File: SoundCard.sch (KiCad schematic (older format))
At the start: 44 parts, among them J1 Conn_Coaxial_inv, J2 Conn_01x03_Female, J3 Conn_01x03_Female, P1 CONN_36_P1.00_PCI, U1 LM334M, U2 LM1972, U3 OPA2388IDGK, U4 TLV320ADC6140, U5 TPS7A90

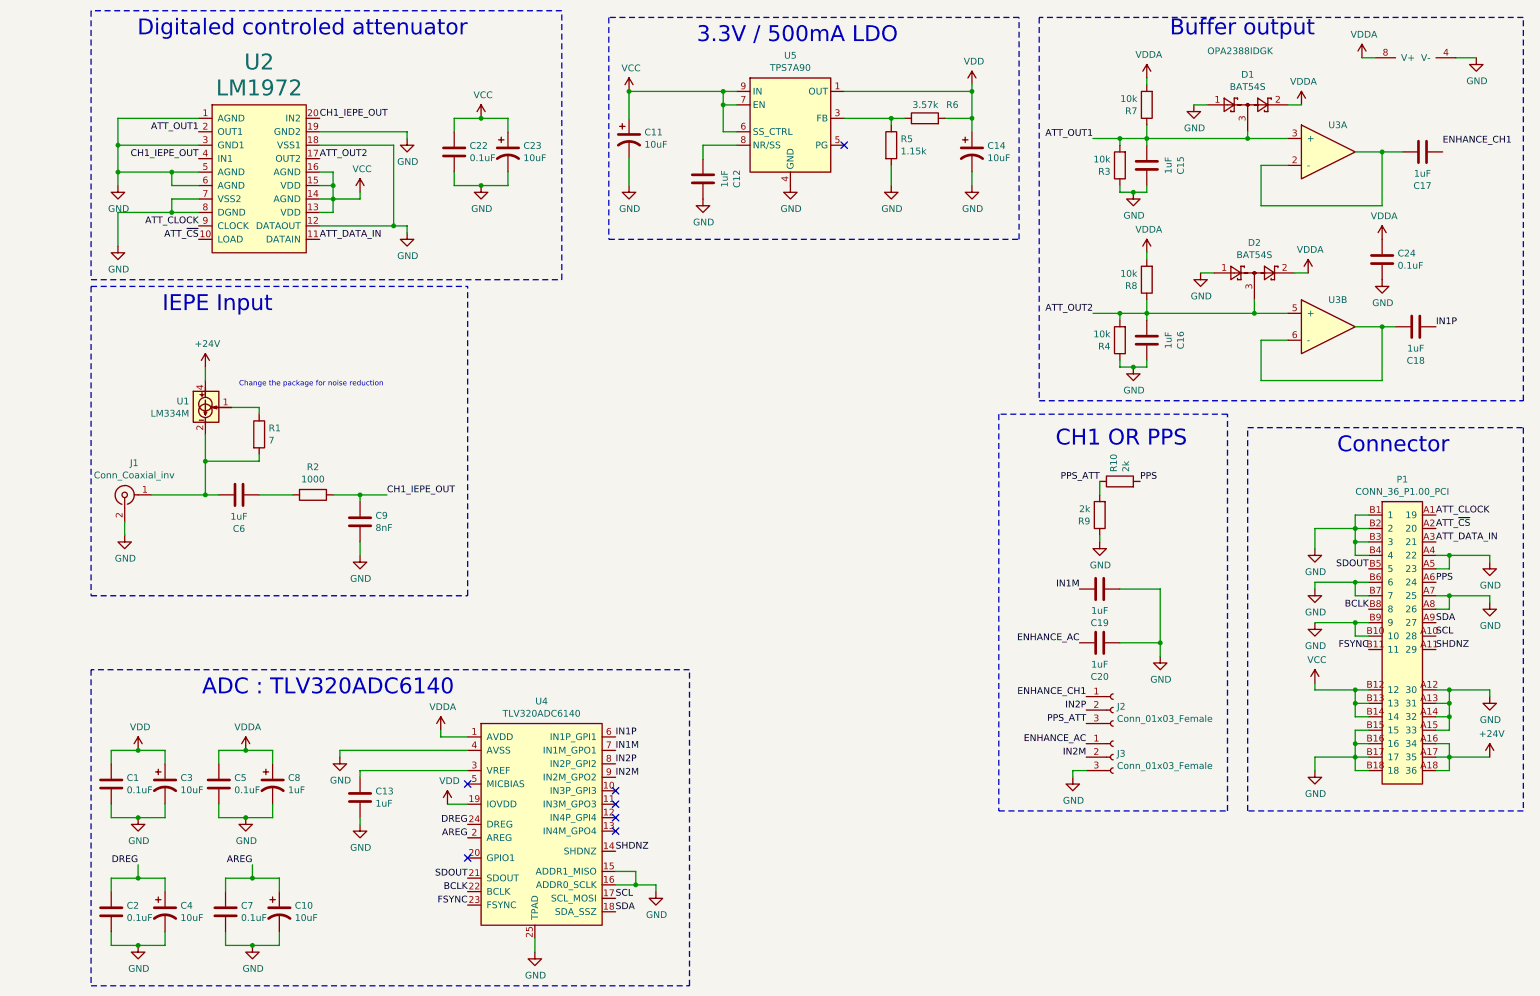
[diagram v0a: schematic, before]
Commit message: Adding 1.65V LDO for Recommon voltage of AOP
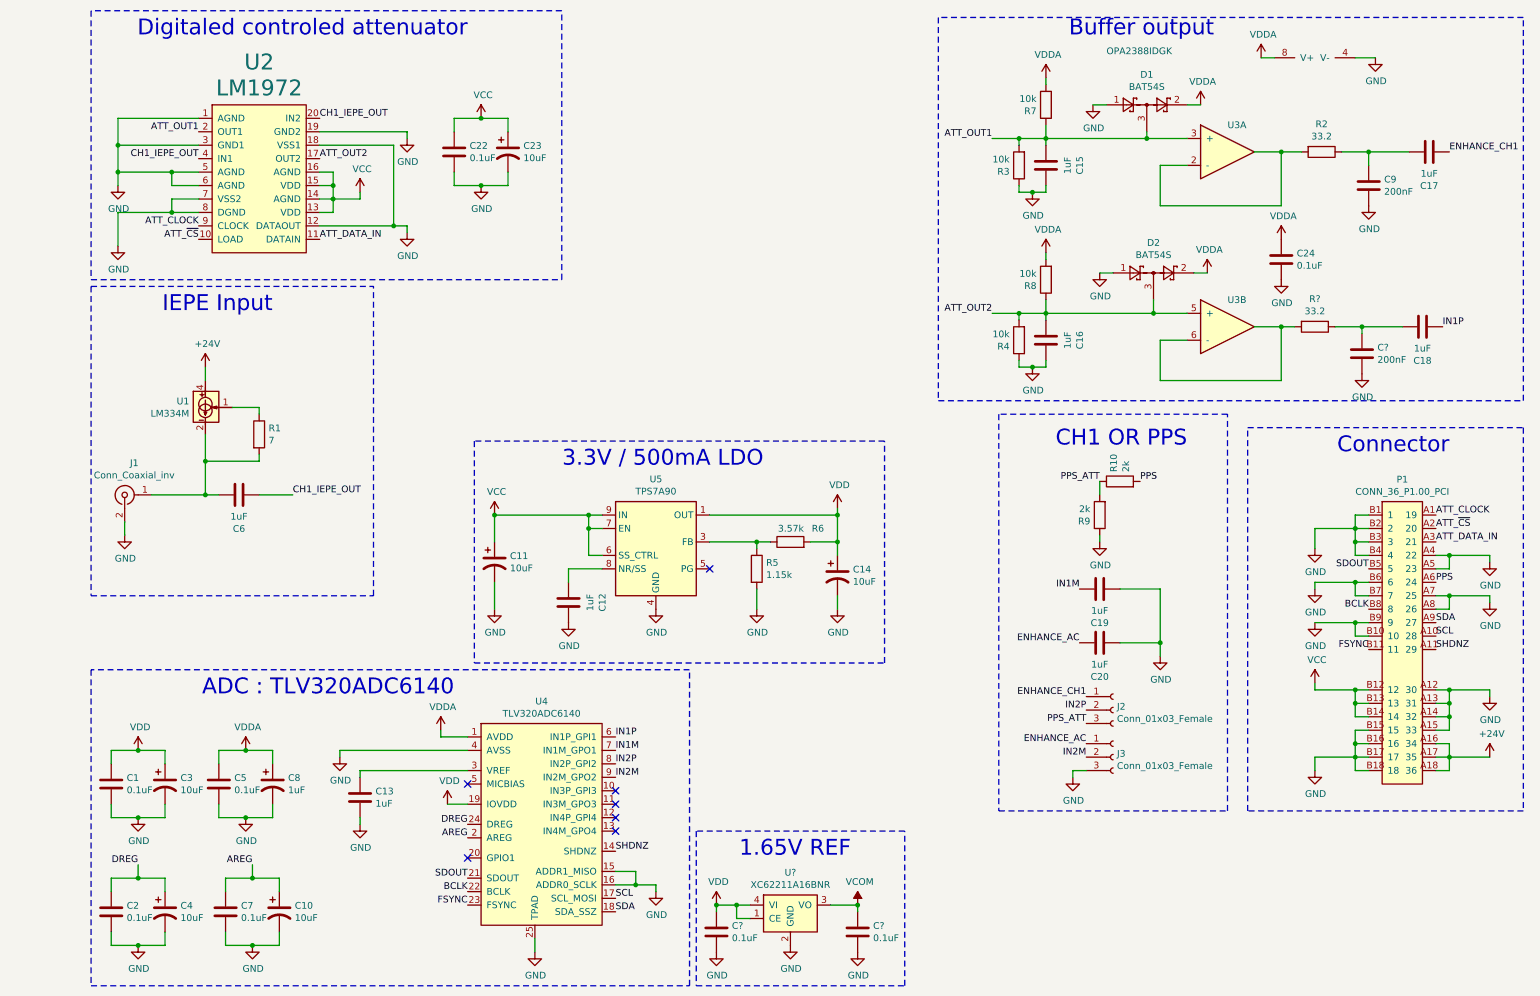
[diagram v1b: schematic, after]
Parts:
- added C?: 200nF, Capacitor_SMD:C_0402_1005Metric, symbol Device:C
- added C? (x2): 0.1uF, Capacitor_SMD:C_0402_1005Metric, symbol Device:C
- added R?: 33.2, Resistor_SMD:R_0402_1005Metric, symbol Device:R
- added U?: XC62211A16BNR, Audio_perso:SSOT-24, symbol Audio_persolib:XC62211A16BNR
- C9: value 8nF -> 200nF
- R2: value 1000 -> 33.2
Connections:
- net CH1_IEPE_OUT: now also C6.2; no longer C9.1, R2.1
- net ENHANCE_CH1: now also C17.2
- net GND: now also C?.1, C?.1, C?.2, U?.2 (GND)
- net VDD: now also C?.2, U?.1 (CE), U?.4 (VI)
- net at U3.6 (-), U3.7: now also R?.2; no longer C18.1
- net at U3.1, U3.2 (-): now also R2.2; no longer C17.1
- new net: C17.1, C9.1, R2.1
- new net: C18.1, C?.1, R?.1
- new net VCOM: C?.2, U?.3 (VO)
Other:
- note added: "1.65V REF"
- note removed: "Change the package for noise reduction"
- moved on the sheet: C11, C12, C14, C15, C16, C17, C18, C24, C9, D1, D2, R2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

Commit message: modif suite à test, simplification.
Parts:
- removed C15, C16: 1uF, Capacitor_SMD:C_0402_1005Metric, symbol Device:C
- removed C22, C24: 0.1uF, Capacitor_SMD:C_0402_1005Metric, symbol Device:C
- removed C23: 10uF, Capacitor_SMD:C_0805_2012Metric, symbol Device:CP1
- removed R3, R4, R7, R8: 10k, Resistor_SMD:R_0402_1005Metric, symbol Device:R
- removed U2: LM1972, Package_SO:SOIC-20W_7.5x12.8mm_P1.27mm, symbol Audio_persolib:LM1972
- removed U3: OPA2388IDGK, Package_SO:VSSOP-8_3.0x3.0mm_P0.65mm, symbol Audio_persolib:OPA2388IDGK
- added R?: 1000, Resistor_SMD:R_0402_1005Metric, symbol Device:R
- added R?: 750, Resistor_SMD:R_0402_1005Metric, symbol Device:R
- C6: value 1uF -> 4.7uF
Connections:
- net ATT_OUT1 is gone; now on net IEPE_OUT: D1.3
- net ATT_OUT2 is gone; now on net IEPE_OUT_ATT: D2.3
- net CH1_IEPE_OUT is gone; now on net IEPE_OUT: C6.2
- net GND: now also R?.1
- net VDD: now also C5.2, C8.1, D1.2, D2.2
- net VDDA: no longer C5.2, C8.1, D1.2, D2.2
- net IEPE_OUT_ATT: now reaches R?.2
- net IEPE_OUT_ATT: now also R?.1, R?.2
- net IEPE_OUT: now reaches R2.2
- net IEPE_OUT: now also R?.2
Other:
- note removed: "Buffer output"
- note removed: "Digitaled controled attenuator"
- moved on the sheet: C11, C12, C14, D1, D2, R5, R6, U5

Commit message: routage terminé
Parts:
- removed C? (x2): 0.1uF, Capacitor_SMD:C_0402_1005Metric, symbol Device:C
- removed U?: XC62211A16BNR, Audio_perso:SSOT-24, symbol Audio_persolib:XC62211A16BNR
- added J2: Conn_01x02_Female, Jumper:SolderJumper-2_P1.3mm_Bridged_Pad1.0x1.5mm, symbol Connector:Conn_01x02_Female
- C9: renamed from C6; footprint Capacitor_SMD:C_0402_1005Metric -> Capacitor_SMD:C_0805_2012Metric
- R1: footprint Resistor_SMD:R_0805_2012Metric -> Resistor_SMD:R_0603_1608Metric
- U3: renamed from U4; footprint Package_DFN_QFN:Texas_S-PWQFN-N24_EP2.7x2.7mm -> Package_DFN_QFN:Texas_S-PWQFN-N24_EP2.7x2.7mm_ThermalVias
- gave numbers to parts that had none: 4
- renumbered C11 to C1, C8 to C10, C10 to C11, C13 to C12, C14 to C13, C9 to C14, C18 to C16, C19 to C18, C20 to C19, C1 to C2, C2 to C3, C3 to C4, C4 to C5, C12 to C6, C5 to C7, C7 to C8, J2 to J3, J3 to J4, R5 to R4, R6 to R5, R2 to R7, R9 to R8, R10 to R9, U5 to U2
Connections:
- net ATT_CLOCK is gone; now on net SHDNZ: P1.A1 (19)
- net ATT_DATA_IN is gone; now on net SDA: P1.A3 (21)
- net ATT_~CS~ is gone; now on net SCL: P1.A2 (20)
- net VDDA is gone; now on net VDD: U3.1 (AVDD)
- net GND: now also P1.A10 (28), P1.A11 (29), P1.A9 (27), P1.B12 (12), P1.B13 (13), P1.B14 (14); no longer P1.B16 (16), P1.B17 (17), P1.B18 (18)
- net SCL: no longer P1.A10 (28)
- net SDA: no longer P1.A9 (27)
- net SHDNZ: no longer P1.A11 (29)
- net VCC: now also P1.B16 (16), P1.B17 (17), P1.B18 (18); no longer P1.B12 (12), P1.B13 (13), P1.B14 (14)
- net at R1.2, U1.2, U1.3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: now also J2.1 (Pin_1); no longer C9.1, J1.1 (Ext)
- new net: C9.1, J1.1 (Ext), J2.2 (Pin_2)
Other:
- note added: "Low pass filter"
- note added: "Note: change the IEPE alim with a \ncurrent mirror to increase the current."
- note removed: "1.65V REF"
- moved on the sheet: C1, C10, C13, C14, C15, C16, C17, C18, C19, C6, C7, C9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
